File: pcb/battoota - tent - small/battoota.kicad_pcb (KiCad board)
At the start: 2 copper layers, 119.1 x 92.5 mm, 38 parts

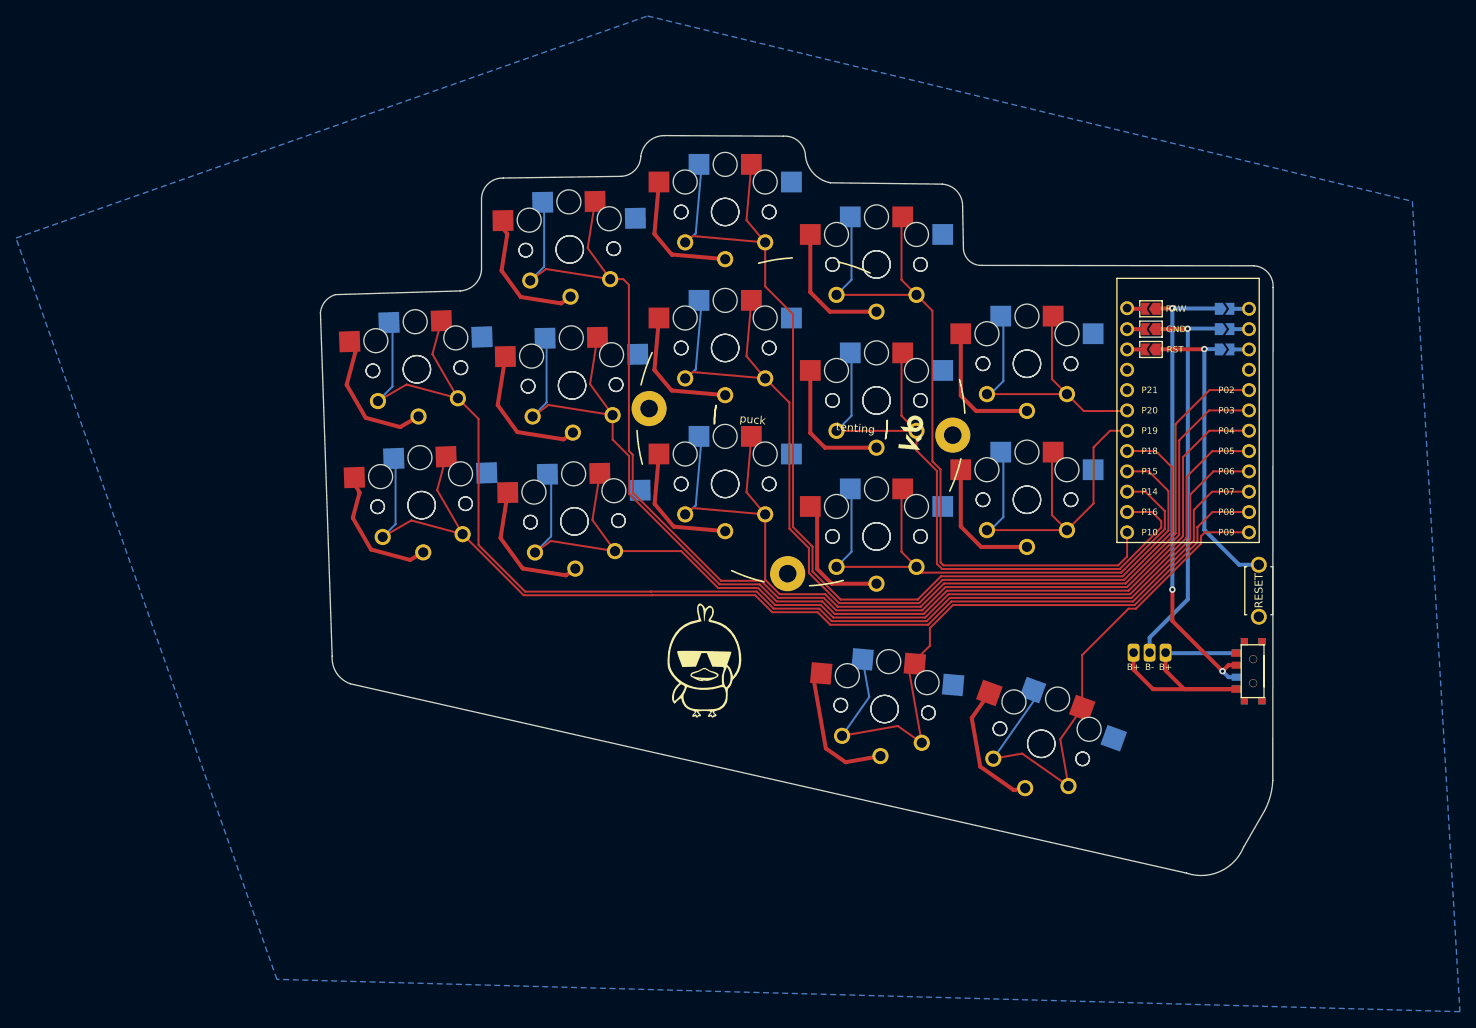
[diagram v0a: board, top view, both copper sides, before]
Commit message: batta tenting improve shape
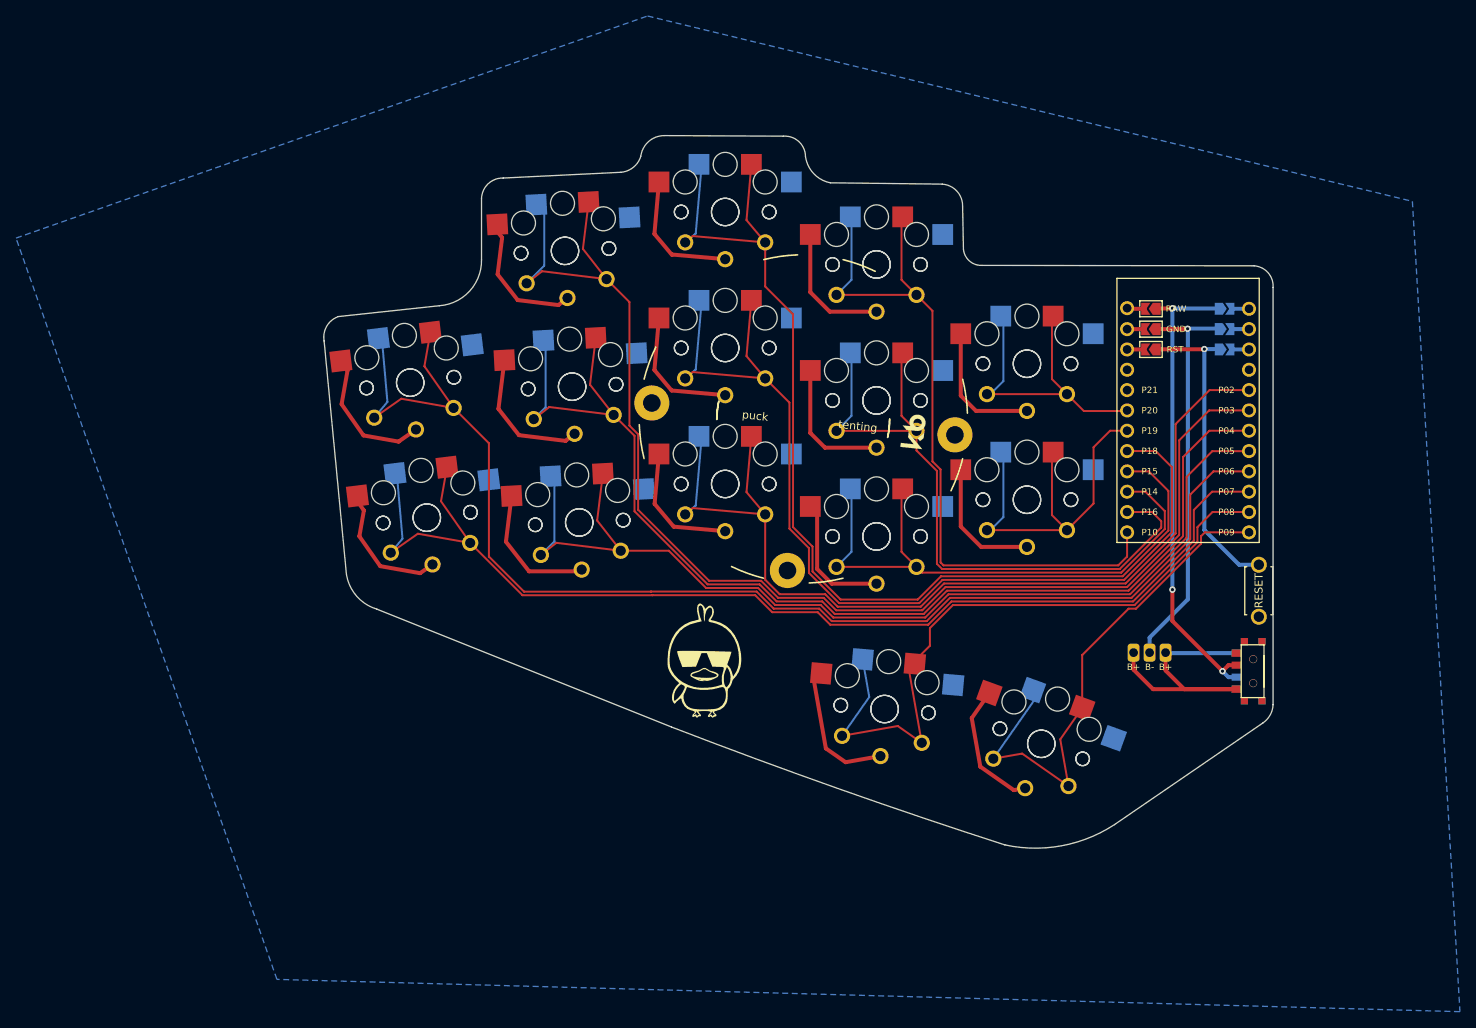
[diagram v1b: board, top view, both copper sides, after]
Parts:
- moved S5 1.87 mm to (57.1, -91.9), turned to 7 degrees
- moved S6 1.87 mm to (57.1, -91.9), turned to -173 degrees
- moved S3 1.68 mm to (59.2, -75.0), turned to 7 degrees
- moved S4 1.68 mm to (59.2, -75.0), turned to -173 degrees
- moved S11 0.62 mm to (76.5, -108.4), turned to 3 degrees
- moved S12 0.62 mm to (76.5, -108.4), turned to -177 degrees
- moved S7 0.61 mm to (78.3, -74.4), turned to 3 degrees
- moved S8 0.61 mm to (78.3, -74.4), turned to -177 degrees
- moved REF** 0.48 mm to (106.3, -87.4), turned to 84 degrees
- moved S10 0.15 mm to (77.4, -91.4), turned to -177 degrees
- moved S9 0.15 mm to (77.4, -91.4), turned to 3 degrees
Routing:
- net P7: track 144.2 -> 142.8 mm
- net P6: track 162.9 -> 162.0 mm
- net P4: track 141.5 -> 142.4 mm
- net P5: track 127.8 -> 127.0 mm
- net P3: track 161.0 -> 161.7 mm
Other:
- board size 119.1 x 92.5 mm -> 118.7 x 89.1 mm
